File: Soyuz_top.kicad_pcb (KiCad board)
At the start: 2 copper layers, 265.4 x 111.2 mm, 47 parts, among them SW1 SW_Push, U1 ProMicro

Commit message: Updating outlines
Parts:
- removed D1, D10, D11, D12, D13, D14, D15, D16, D17, D18, D19, D2, D20, D3, D4, D5, D6, D7, D8, D9: 1N4148, Diodes_THT:D_DO-35_SOD27_P7.62mm_Horizontal
- removed G***: LOGO, locallib:ai-ring-25mm-mask
- removed MX1, MX10, MX11, MX12, MX13, MX14, MX15, MX16, MX17, MX19, MX2, MX20, MX21, MX22, MX3, MX4, MX5, MX6, MX7, MX8: MX-1U, MX_Alps_Hybrid:MX-1U-NoLED
- removed MX18, MX23, MX9: MX-2U, MX_Alps_Hybrid:MX-2U-ReversedStabilizers-NoLED
- removed O1: Outline, locallib:outline
- removed SW1: SW_Push, random-keyboard-parts:PushButton_6x6mm_TH_Pretty
- removed U1: ProMicro, promicro:ProMicro-EnforcedTop
- added REF**: outline_top, locallib:outline_top, F.Cu at (200.7, 133.3)
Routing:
- net ROW4: track 114.9 -> 0.00 mm
- net COL3: track 112.9 -> 0.00 mm
- net COL0: track 99.4 -> 0.00 mm
- net ROW3: track 92.6 -> 0.00 mm
- net COL1: track 91.9 -> 0.00 mm
- net COL2: track 87.5 -> 0.00 mm
- net ROW0: track 85.3 -> 0.00 mm
- net ROW1: track 84.2 -> 0.00 mm
- net GND: track 78.2 -> 0.00 mm
- net ROW2: track 72.7 -> 0.00 mm
- net Net-(SW1-Pad1): track 48.8 -> 0.00 mm
- net Net-(D2-Pad2): track 34.8 -> 0.00 mm
- net Net-(D6-Pad2): track 28.1 -> 0.00 mm
- net Net-(D11-Pad2): track 25.4 -> 0.00 mm
- net Net-(D12-Pad2): track 25.3 -> 0.00 mm
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- removed copper zone on B.Cu, net GNDA
- removed copper zone on F.Cu, net GNDA
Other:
- board size 265.4 x 111.2 mm -> 92.2 x 111.2 mm
- board text removed: "Pro Micro Component side faces away from PCB"
- board text removed: "Soyuz PCB R1.0 20190113"
- board text removed: "Vendor/Customizing instructions 1. Fork Soyuz on GitHub to create your own copy. Clone onto your PC. 2. Turn your logo into a footprint using bitmap2component, save in locallib.pretty. 3. Place it on the topside of the bottom plate. It is left intentionally blank for this. 4. Alt+3 to render and see if it looks nice. 5. Using the Plot tool, generate the gerbers. The bottom plate is reversible."
- board text removed: "kb.ai03.me"

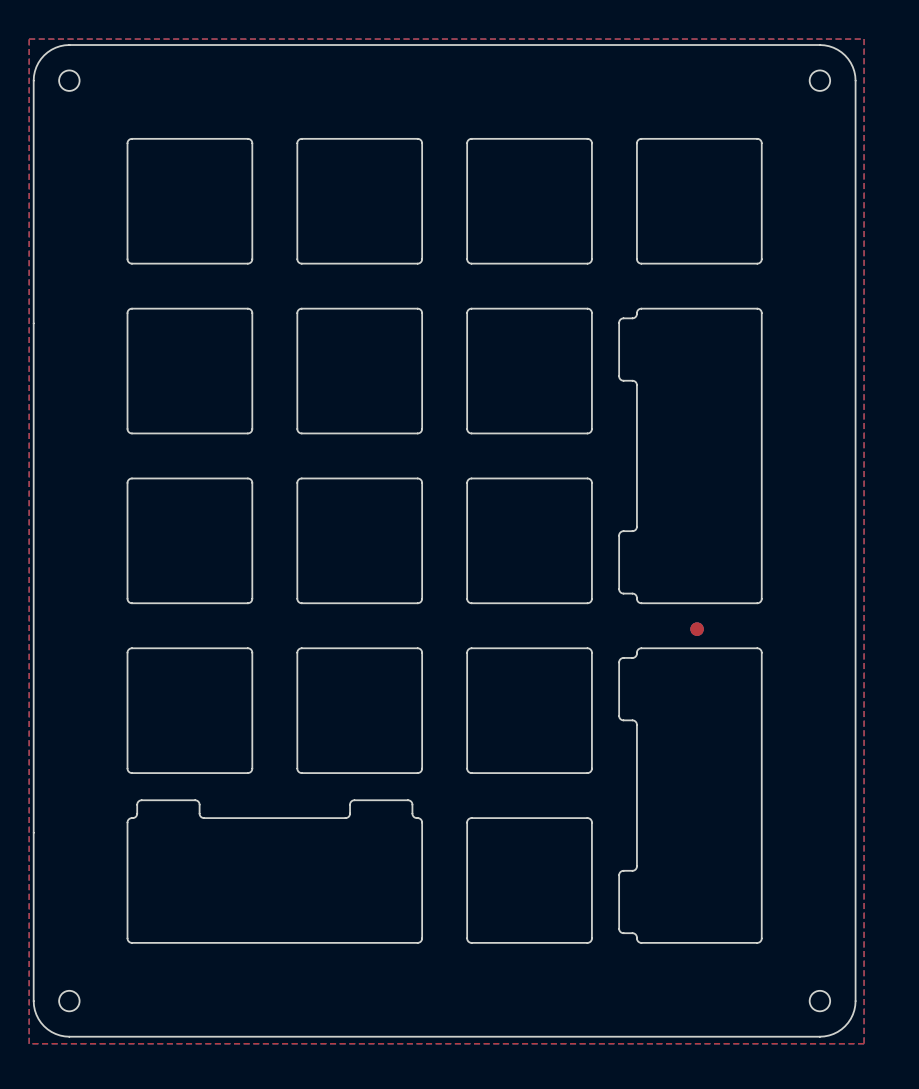
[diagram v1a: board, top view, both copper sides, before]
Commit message: Added copper pour to top plate.
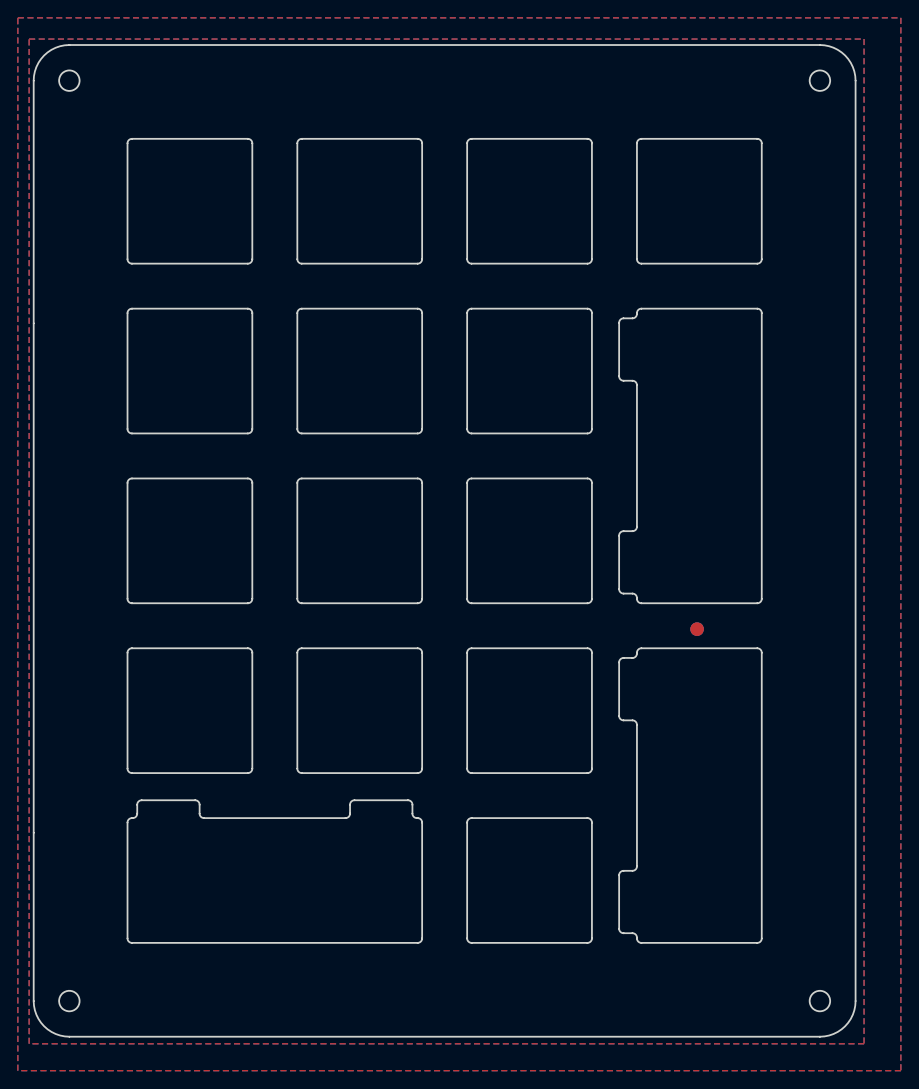
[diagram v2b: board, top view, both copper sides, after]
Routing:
- added copper zone on B.Cu, net (none)
- added copper zone on F.Cu, net (none)
